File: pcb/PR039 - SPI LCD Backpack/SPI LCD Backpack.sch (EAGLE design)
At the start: 15 parts, among them IC1 74HC595D, T1 BC847, T2 BC847, T3 BC847, X1 22-23-2081

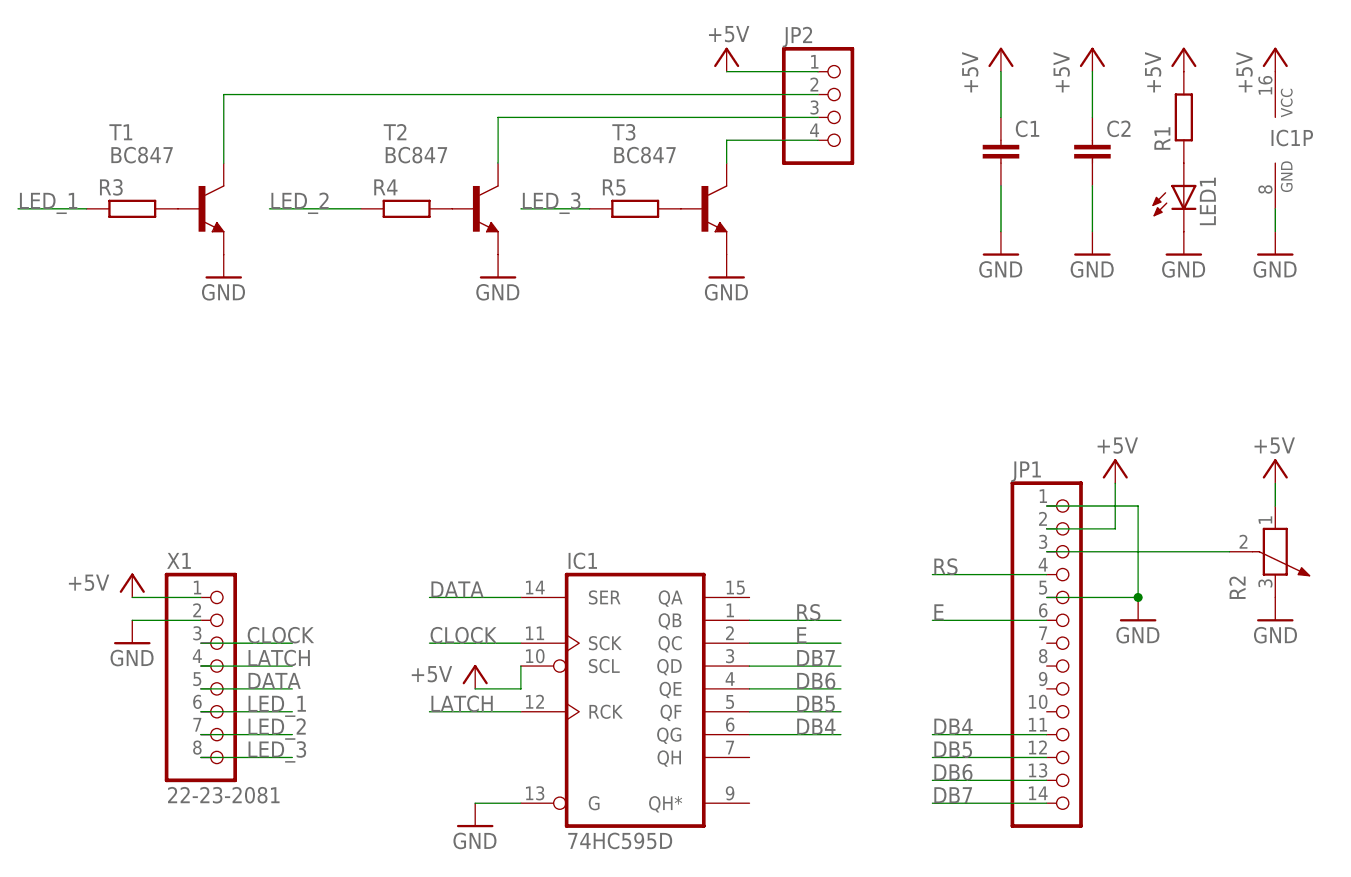
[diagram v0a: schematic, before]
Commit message: 
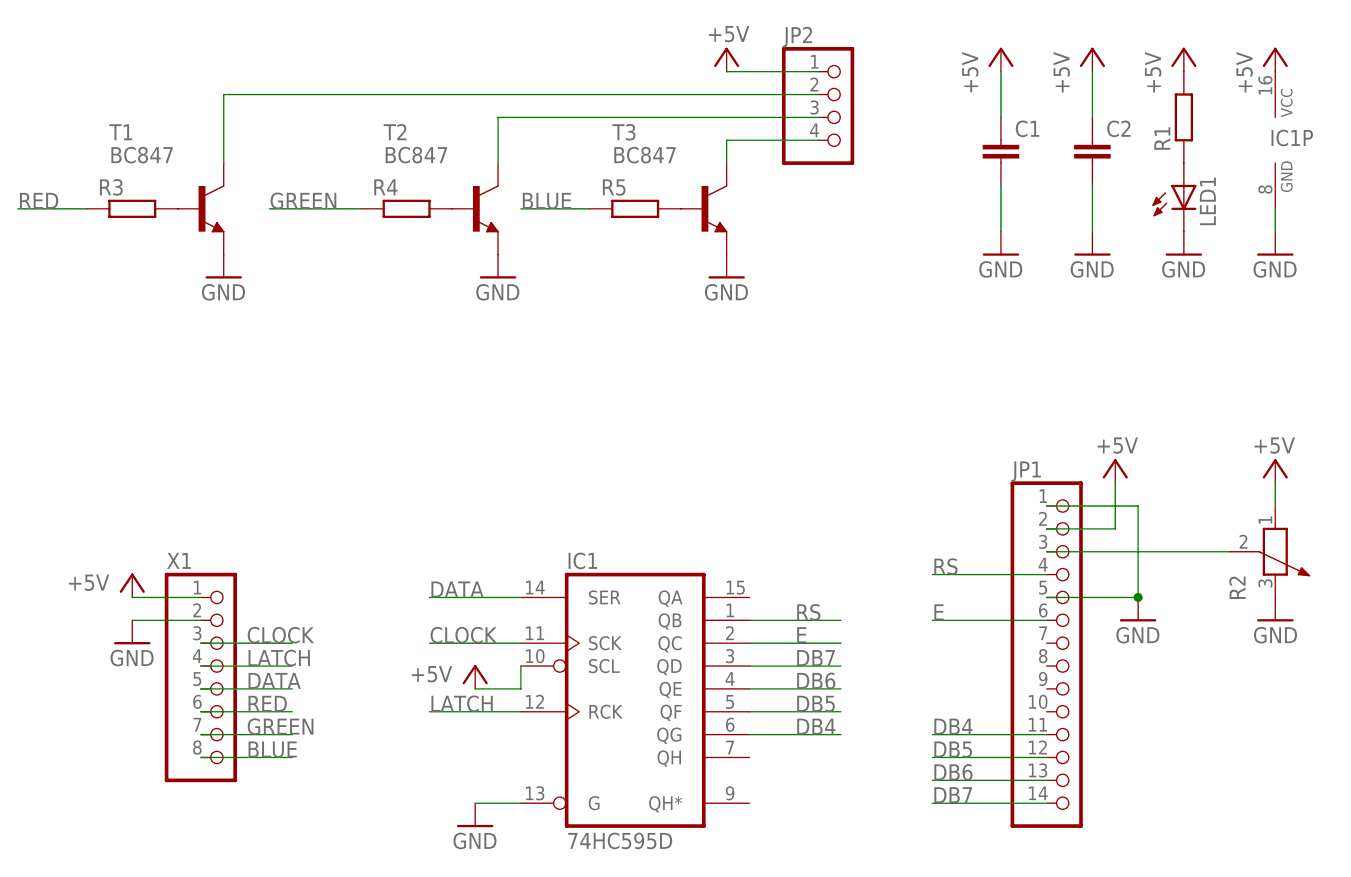
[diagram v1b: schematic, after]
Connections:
- net LED_1 renamed RED
- net LED_2 renamed GREEN
- net LED_3 renamed BLUE
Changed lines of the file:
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@@
 <?xml version="1.0" encoding="utf-8"?>
 <!DOCTYPE eagle SYSTEM "eagle.dtd">
-<eagle version="6.6.0">
+<eagle version="6.5.0">
 <drawing>
 <settings>
@@
 <part name="GND10" library="SPI LCD Backpack" deviceset="GND" device=""/>
 <part name="GND11" library="SPI LCD Backpack" deviceset="GND" device=""/>
-<part name="X1" library="SPI LCD Backpack" deviceset="22-23-2081" device="" value="22-23-2081"/>
+<part name="X1" library="SPI LCD Backpack" deviceset="22-23-2081" device="" value=""/>
 </parts>
 <sheets>
@@
 </segment>
 </net>
-<net name="LED_1" class="0">
+<net name="RED" class="0">
 <segment>
 <pinref part="R3" gate="G$1" pin="1"/>
@@
 </segment>
 </net>
-<net name="LED_2" class="0">
+<net name="GREEN" class="0">
 <segment>
 <pinref part="R4" gate="G$1" pin="1"/>
@@
 </segment>
 </net>
-<net name="LED_3" class="0">
+<net name="BLUE" class="0">
 <segment>
 <pinref part="R5" gate="G$1" pin="1"/>

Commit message: 
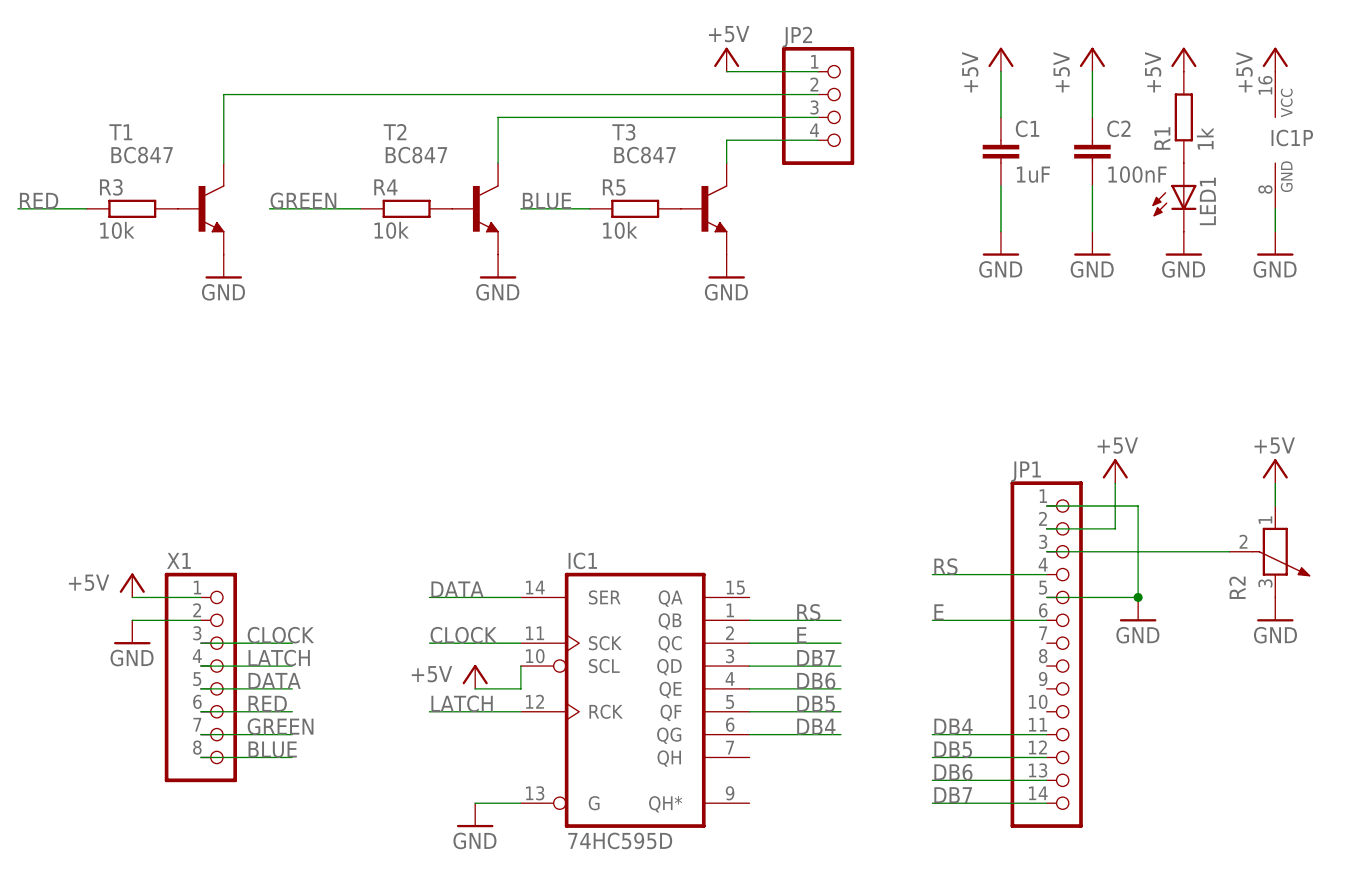
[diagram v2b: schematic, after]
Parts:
- C1: value (none) -> 1uF
- C2: value (none) -> 100nF
- R1: value (none) -> 1k
- R3, R4, R5: value (none) -> 10k
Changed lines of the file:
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@@
 <?xml version="1.0" encoding="utf-8"?>
 <!DOCTYPE eagle SYSTEM "eagle.dtd">
-<eagle version="6.5.0">
+<eagle version="7.1.0">
 <drawing>
 <settings>
@@
 <parts>
 <part name="P+1" library="SPI LCD Backpack" deviceset="+5V" device=""/>
-<part name="C1" library="SPI LCD Backpack" deviceset="C-EU" device="C0805K"/>
-<part name="R1" library="SPI LCD Backpack" deviceset="R-EU_" device="0805"/>
+<part name="C1" library="SPI LCD Backpack" deviceset="C-EU" device="C0805K" value="1uF"/>
+<part name="R1" library="SPI LCD Backpack" deviceset="R-EU_" device="0805" value="1k"/>
 <part name="IC1" library="SPI LCD Backpack" deviceset="74*595" device="D" technology="HC"/>
 <part name="GND1" library="SPI LCD Backpack" deviceset="GND" device=""/>
@@
 <part name="GND4" library="SPI LCD Backpack" deviceset="GND" device=""/>
 <part name="P+6" library="SPI LCD Backpack" deviceset="+5V" device=""/>
-<part name="C2" library="SPI LCD Backpack" deviceset="C-EU" device="C0805K"/>
+<part name="C2" library="SPI LCD Backpack" deviceset="C-EU" device="C0805K" value="100nF"/>
 <part name="GND5" library="SPI LCD Backpack" deviceset="GND" device=""/>
 <part name="P+7" library="SPI LCD Backpack" deviceset="+5V" device=""/>
 <part name="R2" library="SPI LCD Backpack" deviceset="POTENTIOMETER_" device="3386F"/>
 <part name="GND6" library="SPI LCD Backpack" deviceset="GND" device=""/>
-<part name="R3" library="SPI LCD Backpack" deviceset="R-EU_" device="0805"/>
+<part name="R3" library="SPI LCD Backpack" deviceset="R-EU_" device="0805" value="10k"/>
 <part name="T1" library="SPI LCD Backpack" deviceset="BC847" device=""/>
 <part name="GND7" library="SPI LCD Backpack" deviceset="GND" device=""/>
-<part name="R4" library="SPI LCD Backpack" deviceset="R-EU_" device="0805"/>
+<part name="R4" library="SPI LCD Backpack" deviceset="R-EU_" device="0805" value="10k"/>
 <part name="T2" library="SPI LCD Backpack" deviceset="BC847" device=""/>
 <part name="GND8" library="SPI LCD Backpack" deviceset="GND" device=""/>
-<part name="R5" library="SPI LCD Backpack" deviceset="R-EU_" device="0805"/>
+<part name="R5" library="SPI LCD Backpack" deviceset="R-EU_" device="0805" value="10k"/>
 <part name="T3" library="SPI LCD Backpack" deviceset="BC847" device=""/>
 <part name="GND9" library="SPI LCD Backpack" deviceset="GND" device=""/>
